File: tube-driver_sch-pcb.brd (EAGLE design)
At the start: 100 x 100 mm, 132 parts, among them CN1 KS 54, CN10 NO FIT, CN2 MUSB-05-S-B-SM-A, CN3 KS 54, CN4 KS 54, CN5 KS 54, CN6 KS 54, CN7 KS 54, CN8 KS 54, CN9 KS 54, Q4 MMBT3904, Q5 MMBT3904, SW1 RA SM TACT, SW2 RA SM TACT, SW3 RA SM TACT, U1 STM32L052C8, U10 TPS61500, U11 3.3V BUCK, U2 TPS61500, U3 TPS61500, U5 ESP32, U6 USBLC6-2SC6, U7 FT231X, U8 TPS61500

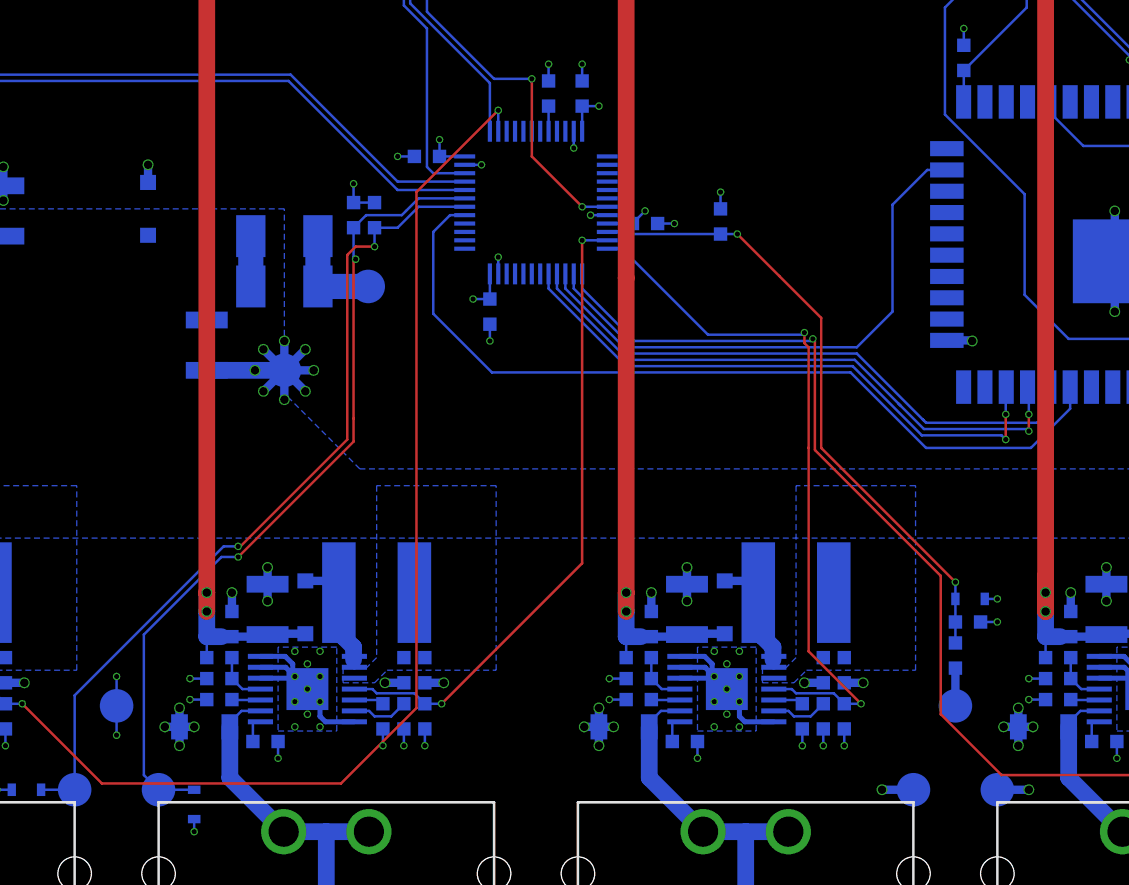
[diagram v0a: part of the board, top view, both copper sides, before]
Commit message: Driver passes DRC ready to create outputs
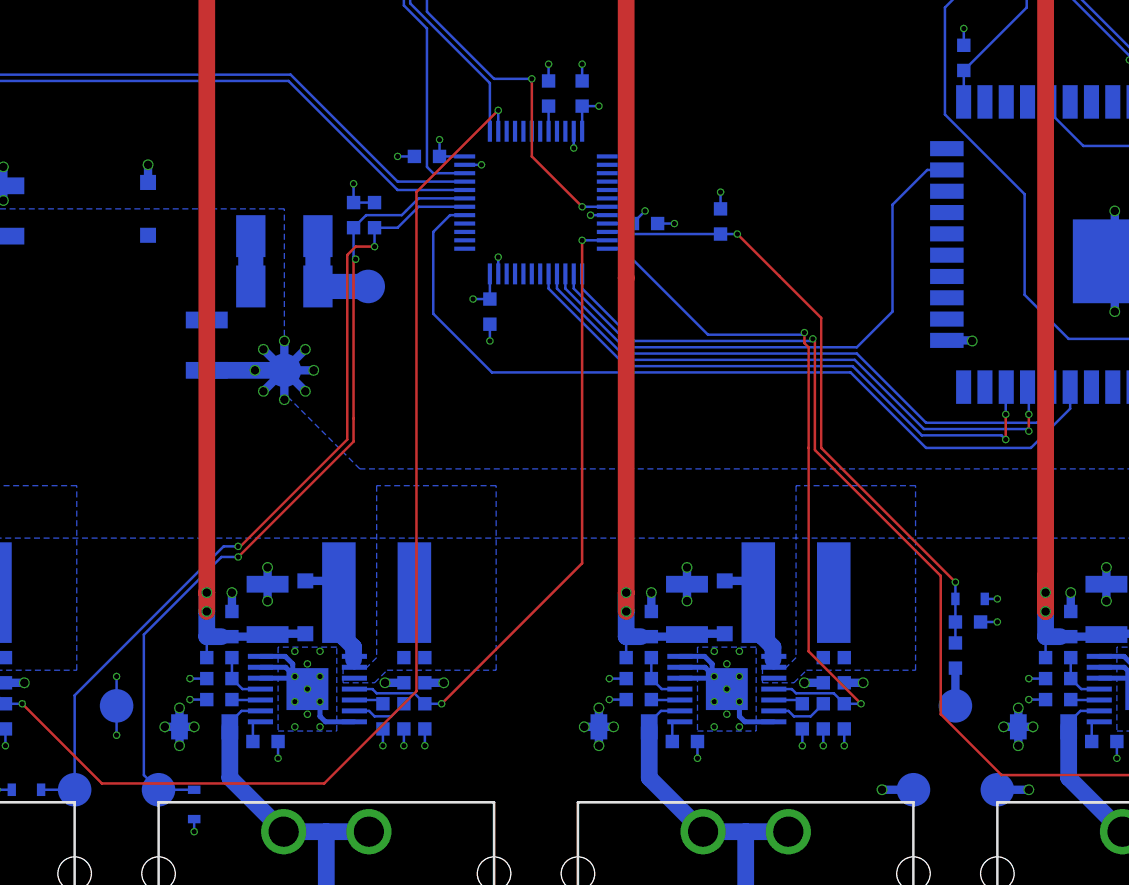
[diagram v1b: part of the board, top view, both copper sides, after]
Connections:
- removed net LED_PWM: U5.28
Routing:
- net LED_PWM_0: track 71.8 -> 71.2 mm
- net LED_PWM: track 0.58 -> 0.00 mm
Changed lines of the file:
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@@
 <?xml version="1.0" encoding="utf-8"?>
 <!DOCTYPE eagle SYSTEM "eagle.dtd">
-<eagle version="9.3.2">
+<eagle version="9.3.0">
 <drawing>
 <settings>
-<setting alwaysvectorfont="yes"/>
+<setting alwaysvectorfont="no"/>
 <setting verticaltext="up"/>
 </settings>
@@
 <via x="61" y="50.625" extent="1-16" drill="0.3"/>
 </signal>
-<signal name="LED_PWM">
-<contactref element="U5" pad="28"/>
-<wire x1="79.3" y1="55.425" x2="79.3" y2="56" width="0.15" layer="16"/>
-</signal>
 <signal name="3V3">
 <contactref element="U5" pad="2"/>
@@
 <via x="19.375" y="20.125" extent="1-16" drill="0.3"/>
 <wire x1="19.375" y1="20.125" x2="24.125" y2="15.375" width="0.15" layer="1"/>
-<wire x1="38.375" y1="15.375" x2="42.875" y2="19.875" width="0.15" layer="1"/>
-<wire x1="24.125" y1="15.375" x2="38.375" y2="15.375" width="0.15" layer="1"/>
+<wire x1="37.375" y1="15.375" x2="42.875" y2="20.875" width="0.15" layer="1"/>
+<wire x1="24.125" y1="15.375" x2="37.375" y2="15.375" width="0.15" layer="1"/>
 <wire x1="42.875" y1="50.625" x2="47.75" y2="55.5" width="0.15" layer="1"/>
 <via x="47.75" y="55.5" extent="1-16" drill="0.3"/>
 <wire x1="47.75" y1="55.5" x2="47.75" y2="54.25" width="0.15" layer="16"/>
-<wire x1="42.875" y1="19.875" x2="42.875" y2="50.625" width="0.15" layer="1"/>
+<wire x1="42.875" y1="20.875" x2="42.875" y2="50.625" width="0.15" layer="1"/>
 </signal>
 <signal name="LED_PWM_1">
@@
 <contactref element="U5" pad="10"/>
 <wire x1="51.75" y1="45.75" x2="51.75" y2="44.875" width="0.15" layer="16"/>
-<wire x1="69.125" y1="41" x2="73.0625" y2="37.0625" width="0.15" layer="16"/>
-<wire x1="73.0625" y1="37.0625" x2="73.125" y2="37" width="0.15" layer="16"/>
+<wire x1="69.125" y1="41" x2="73.25" y2="36.875" width="0.15" layer="16"/>
 <wire x1="51.75" y1="44.875" x2="55.625" y2="41" width="0.15" layer="16"/>
 <wire x1="55.625" y1="41" x2="69.125" y2="41" width="0.15" layer="16"/>
-<wire x1="73.0625" y1="37.0625" x2="73.25" y2="36.875" width="0.15" layer="16"/>
 <wire x1="73.25" y1="36.875" x2="79.875" y2="36.875" width="0.15" layer="16"/>
 <wire x1="79.875" y1="36.875" x2="80.57" y2="37.57" width="0.15" layer="16"/>
@@
 <contactref element="U5" pad="11"/>
 <wire x1="51.25" y1="45.75" x2="51.25" y2="44.875" width="0.15" layer="16"/>
-<wire x1="69" y1="40.625" x2="71.625" y2="38" width="0.15" layer="16"/>
-<wire x1="71.625" y1="38" x2="71.75" y2="37.875" width="0.15" layer="16"/>
+<wire x1="69" y1="40.625" x2="73.125" y2="36.5" width="0.15" layer="16"/>
 <wire x1="51.25" y1="44.875" x2="55.5" y2="40.625" width="0.15" layer="16"/>
 <wire x1="55.5" y1="40.625" x2="69" y2="40.625" width="0.15" layer="16"/>
-<wire x1="71.625" y1="38" x2="73.125" y2="36.5" width="0.15" layer="16"/>
 <via x="79.375" y="36.375" extent="1-16" drill="0.3"/>
 <wire x1="79.375" y1="36.375" x2="79.375" y2="37.375" width="0.15" layer="1"/>

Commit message: Changing ESP32 and STM32 interface to UART
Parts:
- removed D10, D9: PESD5Z3.3, DIODES:SC-79
- removed R23, R24: 10k, r_0603:0603
- added C33: 100nF 16V, CAPACITORS:0603
- added R32: 10k, r_0603:0603
- added R33: 120R, r_0603:0603
- added U12: SN65HVD75D, ICs:SO8
- renumbered TP3 to TP10, TP4 to TP9, TP5 to TP11
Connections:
- removed net DEBUG_UART_RX: D9.K, R24.1, TP9.1, U1.31
- removed net DEBUG_UART_TX: D10.K, R23.1, TP10.1, U1.30
- removed net ESP_SPI_CS: U1.14, U5.23
- removed net ESP_SPI_MISO: U1.16, U5.11
- removed net ESP_SPI_MOSI: U1.17, U5.12
- removed net ESP_SPI_SCLK: U1.15, U5.10
- removed net ESP_SPI_SS: U5.8
- new net ESP_UART_RX: U1.12
- new net ESP_UART_TX: U1.13
- new net RS485_DE: R32.2, U1.33, U12.2, U12.3
- new net RS485_UART_RX: U1.31, U12.1
- new net RS485_UART_TX: U1.30, U12.4
- new net RS485_USR_A: R33.2, TP9.1, U12.6
- new net RS485_USR_B: R33.1, TP10.1, U12.7
- net 3V3: now also C33.2, U12.8; no longer R23.2, R24.2
- net ESP_INT: now also U1.14; no longer U1.29
- net GND: now also C33.1, R32.1, U12.5; no longer D10.A, D9.A
- net LED_PWM_0: now also U1.15; no longer U1.38
- net LED_PWM_2: now also U1.21; no longer U1.12
- net LED_PWM_3: now also U1.22; no longer U1.13
- net USER_BTN_1: now also U1.18; no longer U1.33
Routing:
- net DEBUG_UART_TX: track 50.0 -> 0.00 mm, vias 2 -> 0
- net DEBUG_UART_RX: track 49.2 -> 0.00 mm, vias 2 -> 0
- net RS485_DE: track 0.00 -> 41.9 mm, vias 0 -> 4
- net RS485_UART_RX: track 0.00 -> 41.9 mm, vias 0 -> 2
- net RS485_UART_TX: track 0.00 -> 39.5 mm, vias 0 -> 2
- net ESP_SPI_MISO: track 35.2 -> 0.00 mm, vias 2 -> 0
- net ESP_SPI_MOSI: track 35.0 -> 0.00 mm, vias 2 -> 0
- net ESP_SPI_SCLK: track 34.7 -> 0.00 mm
- net ESP_SPI_CS: track 32.7 -> 0.00 mm
- net ESP_INT: track 50.7 -> 38.8 mm
- net RS485_USR_B: track 0.00 -> 9.70 mm
- net RS485_USR_A: track 0.00 -> 9.70 mm
- net LED_PWM_0: track 71.2 -> 61.9 mm
- net USER_BTN_1: track 37.8 -> 45.2 mm, vias 0 -> 2
- net LED_PWM_2: track 43.0 -> 47.0 mm
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
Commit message: ESP and STM UART link established
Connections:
- net ESP_UART_RX: now also U5.27
- net ESP_UART_TX: now also U5.28
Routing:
- net ESP_UART_TX: track 0.00 -> 32.2 mm, vias 0 -> 2
- net ESP_UART_RX: track 0.00 -> 29.1 mm, vias 0 -> 2
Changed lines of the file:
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@@
 <?xml version="1.0" encoding="utf-8"?>
 <!DOCTYPE eagle SYSTEM "eagle.dtd">
-<eagle version="9.5.1">
+<eagle version="9.3.2">
 <drawing>
 <settings>
-<setting alwaysvectorfont="no"/>
+<setting alwaysvectorfont="yes"/>
 <setting verticaltext="up"/>
 </settings>
@@
 </layers>
 <board>
-<fusionsync huburn="a.cGVyc29uYWw6dWUyYjllNWFm" projecturn="a.cGVyc29uYWw6dWUyYjllNWFmIzIwMTkxMDE5MjI4NzM0NTgx" f3durn="urn:adsk.wipprod:dm.lineage:UOlpTiM0SG240spYVLI8lw" pcbguid="77afd29c-32cb-411e-83ac-e2ab0f91457c" lastpulledtime="" lastsyncedchangeguid="2c6301ce-06ae-837c-a818-5b95e475ee39"/>
+<fusionsync huburn="a.cGVyc29uYWw6dWUyYjllNWFm" projecturn="a.cGVyc29uYWw6dWUyYjllNWFmIzIwMTkxMDE5MjI4NzM0NTgx" f3durn="urn:adsk.wipprod:dm.lineage:UOlpTiM0SG240spYVLI8lw" pcbguid="77afd29c-32cb-411e-83ac-e2ab0f91457c" lastpulledtime="" lastsyncedchangeguid="424de3ad-c678-a7c8-acd4-f3680f6de184"/>
 <plain>
 <wire x1="97" y1="0" x2="100" y2="3" width="0" layer="20" curve="90"/>
@@
 <signal name="ESP_UART_RX">
 <contactref element="U1" pad="12"/>
+<contactref element="U5" pad="27"/>
+<wire x1="78.03" y1="56" x2="78.03" y2="54.72" width="0.15" layer="16"/>
+<wire x1="78.03" y1="54.72" x2="78.375" y2="54.375" width="0.15" layer="16"/>
+<via x="78.375" y="54.375" extent="1-16" drill="0.3"/>
+<wire x1="78.375" y1="54.375" x2="78.375" y2="54" width="0.15" layer="1"/>
+<wire x1="57.75" y1="47.25" x2="57.5" y2="47.25" width="0.15" layer="1"/>
+<via x="57.5" y="47.25" extent="1-16" drill="0.3"/>
+<wire x1="57.5" y1="47.25" x2="54.25" y2="47.25" width="0.15" layer="16"/>
+<wire x1="78.375" y1="54" x2="73.875" y2="49.5" width="0.15" layer="1"/>
+<wire x1="73.875" y1="49.5" x2="60" y2="49.5" width="0.15" layer="1"/>
+<wire x1="60" y1="49.5" x2="57.75" y2="47.25" width="0.15" layer="1"/>
 </signal>
 <signal name="ESP_UART_TX">
 <contactref element="U1" pad="13"/>
+<contactref element="U5" pad="28"/>
+<wire x1="79.3" y1="56" x2="79.3" y2="54.675" width="0.15" layer="16"/>
+<wire x1="79.3" y1="54.675" x2="79" y2="54.375" width="0.15" layer="16"/>
+<via x="79" y="54.375" extent="1-16" drill="0.3"/>
+<wire x1="79" y1="54.375" x2="79" y2="54.125" width="0.15" layer="1"/>
+<wire x1="79" y1="54.125" x2="74" y2="49.125" width="0.15" layer="1"/>
+<wire x1="60.125" y1="49.125" x2="57.5" y2="46.5" width="0.15" layer="1"/>
+<wire x1="57.5" y1="46.5" x2="57.5" y2="45.75" width="0.15" layer="1"/>
+<via x="57.5" y="45.75" extent="1-16" drill="0.3"/>
+<wire x1="57.5" y1="45.75" x2="52.75" y2="45.75" width="0.15" layer="16"/>
+<wire x1="74" y1="49.125" x2="60.125" y2="49.125" width="0.15" layer="1"/>
 </signal>
 </signals>

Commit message: First revision of the driver complete
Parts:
- added R23, R24: 0R, RESISTORS:0603
- added R34: 5.1k, r_0603:0603
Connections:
- new net ESP_IO13: R23.2, U5.16
- new net ESP_IO15: R24.2, U5.23
- new net N$13: R34.1, U5.24
- net ESP32_UART_!DTR: now also R24.1
- net ESP32_UART_!RTS: now also R23.1
- net GND: now also R34.2
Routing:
- net ESP32_UART_!RTS: track 10.7 -> 42.7 mm
- net ESP32_UART_!DTR: track 10.1 -> 28.8 mm
- net ESP_IO15: track 0.00 -> 1.89 mm
- net ESP_IO13: track 0.00 -> 1.89 mm
- net N$13: track 0.00 -> 1.88 mm
- net GND: track 199.1 -> 200.3 mm, vias 170 -> 171
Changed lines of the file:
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@@
 <?xml version="1.0" encoding="utf-8"?>
 <!DOCTYPE eagle SYSTEM "eagle.dtd">
-<eagle version="9.3.2">
+<eagle version="9.5.1">
 <drawing>
 <settings>
-<setting alwaysvectorfont="yes"/>
+<setting alwaysvectorfont="no"/>
 <setting verticaltext="up"/>
 </settings>
@@
 </layers>
 <board>
-<fusionsync huburn="a.cGVyc29uYWw6dWUyYjllNWFm" projecturn="a.cGVyc29uYWw6dWUyYjllNWFmIzIwMTkxMDE5MjI4NzM0NTgx" f3durn="urn:adsk.wipprod:dm.lineage:UOlpTiM0SG240spYVLI8lw" pcbguid="77afd29c-32cb-411e-83ac-e2ab0f91457c" lastpulledtime="" lastsyncedchangeguid="424de3ad-c678-a7c8-acd4-f3680f6de184"/>
+<fusionsync huburn="a.cGVyc29uYWw6dWUyYjllNWFm" projecturn="a.cGVyc29uYWw6dWUyYjllNWFmIzIwMTkxMDE5MjI4NzM0NTgx" f3durn="urn:adsk.wipprod:dm.lineage:UOlpTiM0SG240spYVLI8lw" pcbguid="77afd29c-32cb-411e-83ac-e2ab0f91457c" lastpulledtime="" lastsyncedchangeguid="dd5d1823-3c66-8cb6-db0c-cc032cee0713"/>
 <plain>
 <wire x1="97" y1="0" x2="100" y2="3" width="0" layer="20" curve="90"/>
@@
 <element name="TP11" library="MISC" package="2MM_TEST_PAD" value="2MM_TEST_POINT" x="25" y="20" smashed="yes" rot="MR0">
 <attribute name="NAME" x="23.375" y="21.125" size="1.27" layer="22" rot="MR270"/>
+</element>
+<element name="R23" library="RESISTORS" package="0603" value="0R" x="71.875" y="43" smashed="yes" rot="MR180">
+<attribute name="DIGIKEY" value="541-0.0GCT-ND" x="71.875" y="43" size="1.778" layer="28" rot="MR180" display="off"/>
+<attribute name="HEIGHT" value="0.5" x="71.875" y="43" size="1.778" layer="28" rot="MR180" display="off"/>
+<attribute name="NAME" x="70.375" y="42.25" size="1.016" layer="26" rot="MR180"/>
+<attribute name="PRICE_PER" value="0.08" x="71.875" y="43" size="1.778" layer="28" rot="MR180" display="off"/>
+</element>
+<element name="R24" library="RESISTORS" package="0603" value="0R" x="71.875" y="52" smashed="yes" rot="MR180">
+<attribute name="DIGIKEY" value="541-0.0GCT-ND" x="71.875" y="52" size="1.778" layer="28" rot="MR180" display="off"/>
+<attribute name="HEIGHT" value="0.5" x="71.875" y="52" size="1.778" layer="28" rot="MR180" display="off"/>
+<attribute name="NAME" x="70.375" y="51.25" size="1.016" layer="26" rot="MR180"/>
+<attribute name="PRICE_PER" value="0.08" x="71.875" y="52" size="1.778" layer="28" rot="MR180" display="off"/>
+</element>
+<element name="R34" library="r_0603" package="0603" value="5.1k" x="71.875" y="53.25" smashed="yes" rot="MR0">
+<attribute name="DIGIKEY" value="P5.10KHCT-ND" x="71.875" y="53.25" size="1.778" layer="28" rot="MR0" display="off"/>
+<attribute name="FARNELL" value="" x="71.875" y="53.25" size="1.778" layer="28" rot="MR0" display="off"/>
+<attribute name="NAME" x="73.375" y="54" size="1.016" layer="26" rot="MR0"/>
+<attribute name="PRICE_PER" value="0.10000" x="71.875" y="53.25" size="1.778" layer="28" rot="MR0" display="off"/>
 </element>
 </elements>
@@
 <wire x1="24.25" y1="31" x2="24.25" y2="32" width="0.15" layer="16"/>
 <via x="24.25" y="32" extent="1-16" drill="0.3"/>
+<contactref element="R34" pad="2"/>
+<wire x1="71.125" y1="53.25" x2="71.125" y2="54.375" width="0.15" layer="16"/>
+<via x="71.125" y="54.375" extent="1-16" drill="0.35"/>
 </signal>
 <signal name="3V3">
@@
 <contactref element="Q4" pad="3"/>
 <contactref element="R22" pad="2"/>
-<wire x1="76.75" y1="68.125" x2="77.625" y2="67.25" width="0.15" layer="16"/>
-<wire x1="77.625" y1="67.25" x2="78.75" y2="67.25" width="0.15" layer="16"/>
-<wire x1="78.75" y1="67.25" x2="79.25" y2="67.75" width="0.15" layer="16"/>
+<wire x1="76.75" y1="68.125" x2="77.5" y2="67.375" width="0.15" layer="16"/>
+<wire x1="77.5" y1="67.375" x2="78.875" y2="67.375" width="0.15" layer="16"/>
+<wire x1="78.875" y1="67.375" x2="79.25" y2="67.75" width="0.15" layer="16"/>
 <wire x1="79.25" y1="67.75" x2="79.25" y2="69.125" width="0.15" layer="16"/>
 <wire x1="79.25" y1="69.125" x2="79.625" y2="69.5" width="0.15" layer="16"/>
 <wire x1="75" y1="72.1525" x2="76.9725" y2="72.1525" width="0.15" layer="16"/>
 <wire x1="76.9725" y1="72.1525" x2="79.625" y2="69.5" width="0.15" layer="16"/>
+<contactref element="R23" pad="1"/>
+<wire x1="75" y1="72.1525" x2="74.2775" y2="72.1525" width="0.15" layer="16"/>
+<wire x1="70" y1="45.375" x2="71.125" y2="44.25" width="0.15" layer="16"/>
+<wire x1="71.125" y1="44.25" x2="71.125" y2="43" width="0.15" layer="16"/>
+<wire x1="74.2775" y1="72.1525" x2="73.875" y2="71.75" width="0.15" layer="16"/>
+<wire x1="73.875" y1="71.75" x2="73.875" y2="62.875" width="0.15" layer="16"/>
+<wire x1="73.875" y1="62.875" x2="70" y2="59" width="0.15" layer="16"/>
+<wire x1="70" y1="59" x2="70" y2="45.375" width="0.15" layer="16"/>
 </signal>
 <signal name="ESP32_UART_!DTR">
@@
 <contactref element="Q5" pad="3"/>
 <contactref element="R21" pad="2"/>
-<wire x1="76.125" y1="69.5" x2="76" y2="69.375" width="0.15" layer="16"/>
-<wire x1="76" y1="67.375" x2="76.5" y2="66.875" width="0.15" layer="16"/>
-<wire x1="79" y1="66.875" x2="80.25" y2="68.125" width="0.15" layer="16"/>
-<wire x1="76" y1="69.375" x2="76" y2="67.375" width="0.15" layer="16"/>
-<wire x1="76.5" y1="66.875" x2="79" y2="66.875" width="0.15" layer="16"/>
+<wire x1="76.125" y1="69.5" x2="75.5" y2="68.875" width="0.15" layer="16"/>
+<wire x1="79.125" y1="67" x2="80.25" y2="68.125" width="0.15" layer="16"/>
+<wire x1="75.5" y1="67" x2="76.375" y2="67" width="0.15" layer="16"/>
+<wire x1="76.375" y1="67" x2="79.125" y2="67" width="0.15" layer="16"/>
 <wire x1="75" y1="71.5175" x2="75.8575" y2="71.5175" width="0.15" layer="16"/>
 <wire x1="75.8575" y1="71.5175" x2="76.125" y2="71.25" width="0.15" layer="16"/>
 <wire x1="76.125" y1="71.25" x2="76.125" y2="69.5" width="0.15" layer="16"/>
+<contactref element="R24" pad="1"/>
+<wire x1="75.5" y1="67" x2="74.875" y2="67" width="0.15" layer="16"/>
+<wire x1="74.875" y1="67" x2="74.25" y2="66.375" width="0.15" layer="16"/>
+<wire x1="70.375" y1="52.75" x2="71.125" y2="52" width="0.15" layer="16"/>
+<wire x1="74.25" y1="66.375" x2="74.25" y2="62.75" width="0.15" layer="16"/>
+<wire x1="74.25" y1="62.75" x2="70.375" y2="58.875" width="0.15" layer="16"/>
+<wire x1="70.375" y1="58.875" x2="70.375" y2="52.75" width="0.15" layer="16"/>
+<wire x1="75.5" y1="68.875" x2="75.5" y2="67.375" width="0.15" layer="16"/>
+<wire x1="75.5" y1="67.375" x2="75.5" y2="67.125" width="0.15" layer="16"/>
+<wire x1="75.5" y1="67.125" x2="75.5" y2="67" width="0.15" layer="16"/>
 </signal>
 <signal name="N$99">
@@
 <wire x1="74" y1="49.125" x2="60.125" y2="49.125" width="0.15" layer="1"/>
 </signal>
+<signal name="ESP_IO13">
+<contactref element="U5" pad="16"/>
+<contactref element="R23" pad="2"/>
+<wire x1="74.49" y1="43.055" x2="72.68" y2="43.055" width="0.15" layer="16"/>
+<wire x1="72.68" y1="43.055" x2="72.625" y2="43" width="0.15" layer="16"/>
+</signal>
+<signal name="ESP_IO15">
+<contactref element="U5" pad="23"/>
+<contactref element="R24" pad="2"/>
+<wire x1="74.49" y1="51.945" x2="72.68" y2="51.945" width="0.15" layer="16"/>
+<wire x1="72.68" y1="51.945" x2="72.625" y2="52" width="0.15" layer="16"/>
+</signal>
+<signal name="N$13">
+<contactref element="U5" pad="24"/>
+<contactref element="R34" pad="1"/>
+<wire x1="74.49" y1="53.215" x2="72.66" y2="53.215" width="0.15" layer="16"/>
+<wire x1="72.66" y1="53.215" x2="72.625" y2="53.25" width="0.15" layer="16"/>
+</signal>
 </signals>
